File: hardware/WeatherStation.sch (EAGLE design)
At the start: 9 parts, among them X2 XRJK-S-01-6-4-0-9M2

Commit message: fixing schematic v1.1
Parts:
- removed BMP280: (no value), pinhead:PINHD-1X6
- removed EXTERN_PINS: (no value), pinhead:PINHD-1X20
- removed U$1: ESP32DEVKITV1, ESP32-DEVKITV1:ESP32DEVKITV1
- removed X2: XRJK-S-01-6-4-0-9M2, con-xmultiplee:XRJK-S-01-6-4-0-9M2
- removed XB2: XBEE-PRO, maxstream:XBEE-PRO
- added ESP32: ESP32DEVKITV1, ESP32-DEVKITV1:ESP32DEVKITV1
- added J2: RJ11, con-rj_fixed:RJ11
- added JP1: (no value), pinhead:PINHD-1X24
- added ROBOCORE_BEE_V2: XBEE-PRO, maxstream:XBEE-PRO
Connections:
- removed net N$13: U$1.IO16, XB2.DOUT
- removed net N$15: U$1.IO5, XB2.!RESET
- new net N$9: ESP32.IO22, JP1.21
- net N$1: now also ESP32.3V3, ESP32.IO34, J2.3, JP1.1, JP1.11, JP1.17, JP1.5, R3.2, ROBOCORE_BEE_V2.VCC; no longer POWER.1, U$1.VIN
- net N$10: now also ESP32.IO21, JP1.23; no longer BMP280.3, U$1.IO22
- net N$11: now also ESP32.IO17, ROBOCORE_BEE_V2.DIN/!CONFIG; no longer BMP280.4, U$1.IO21
- net N$12: now also J2.2, R2.1; no longer U$1.GND@2, XB2.GND
- net N$14: now also J2.1, R3.1; no longer U$1.IO17, XB2.DIN/!CONFIG
- net N$2: now also ESP32.GND@1, ESP32.IO26, J2.4, JP1.13, JP1.19, JP1.3, JP1.7, R2.2; no longer BMP280.2, EXTERN_PINS.13, EXTERN_PINS.3, EXTERN_PINS.9, R3.2, U$1.GND@1, U$1.IO26, X2.1
- net N$3: now also ESP32.IO35, R1.1; no longer BMP280.1, EXTERN_PINS.1, EXTERN_PINS.11, EXTERN_PINS.15, EXTERN_PINS.5, R2.1, U$1.3V3, X2.2, XB2.VCC
- net N$4: now also ESP32.IO15, JP1.9; no longer R1.1, U$1.IO35
- net N$5: now also ESP32.IO16, ROBOCORE_BEE_V2.DOUT; no longer EXTERN_PINS.7, U$1.IO15
- net N$6: now also ESP32.GND@2, ROBOCORE_BEE_V2.GND; no longer EXTERN_PINS.17, U$1.IO4
- net N$7: now also ESP32.IO4, JP1.15; no longer R2.2, U$1.IO34, X2.4
- net N$8: now also ESP32.VIN, POWER.1; no longer R3.1, X2.3
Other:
- note added: "3V3"
- note added: "3V3/EN"
- note added: "Anemometer + Wind Vane"
- note added: "BMP280 BAROMETER"
- note added: "DATA"
- note added: "DHT11 TEMP/HUM SENSOR"
- note added: "GND"
- note added: "GND/DATA"
- note added: "Lucas José da Cunha"
- note added: "OUT"
- note added: "SCL"
- note added: "SDA"
- note added: "VCC"
- note removed: "DHT11 TEMP/HUM"
- note removed: "LUCAS JOSÉ DA CUNHA"
- moved on the sheet: POWER, R2, R3

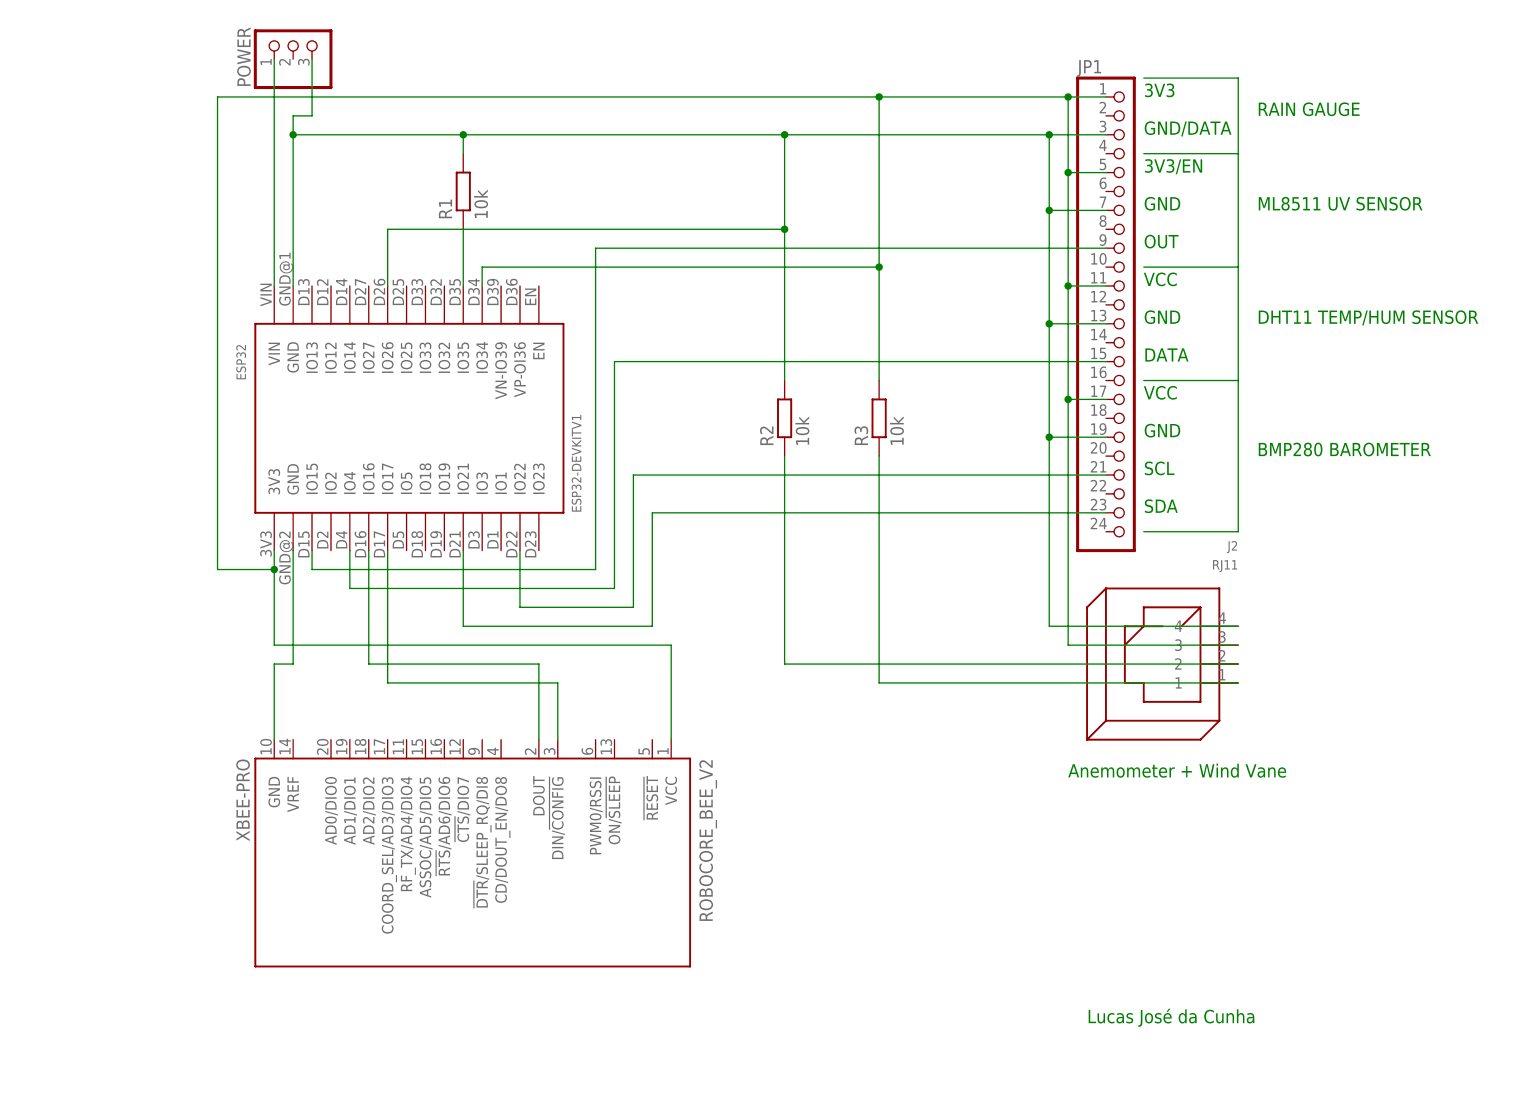
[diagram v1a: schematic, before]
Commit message: changing rain gauge and wind sensor connection
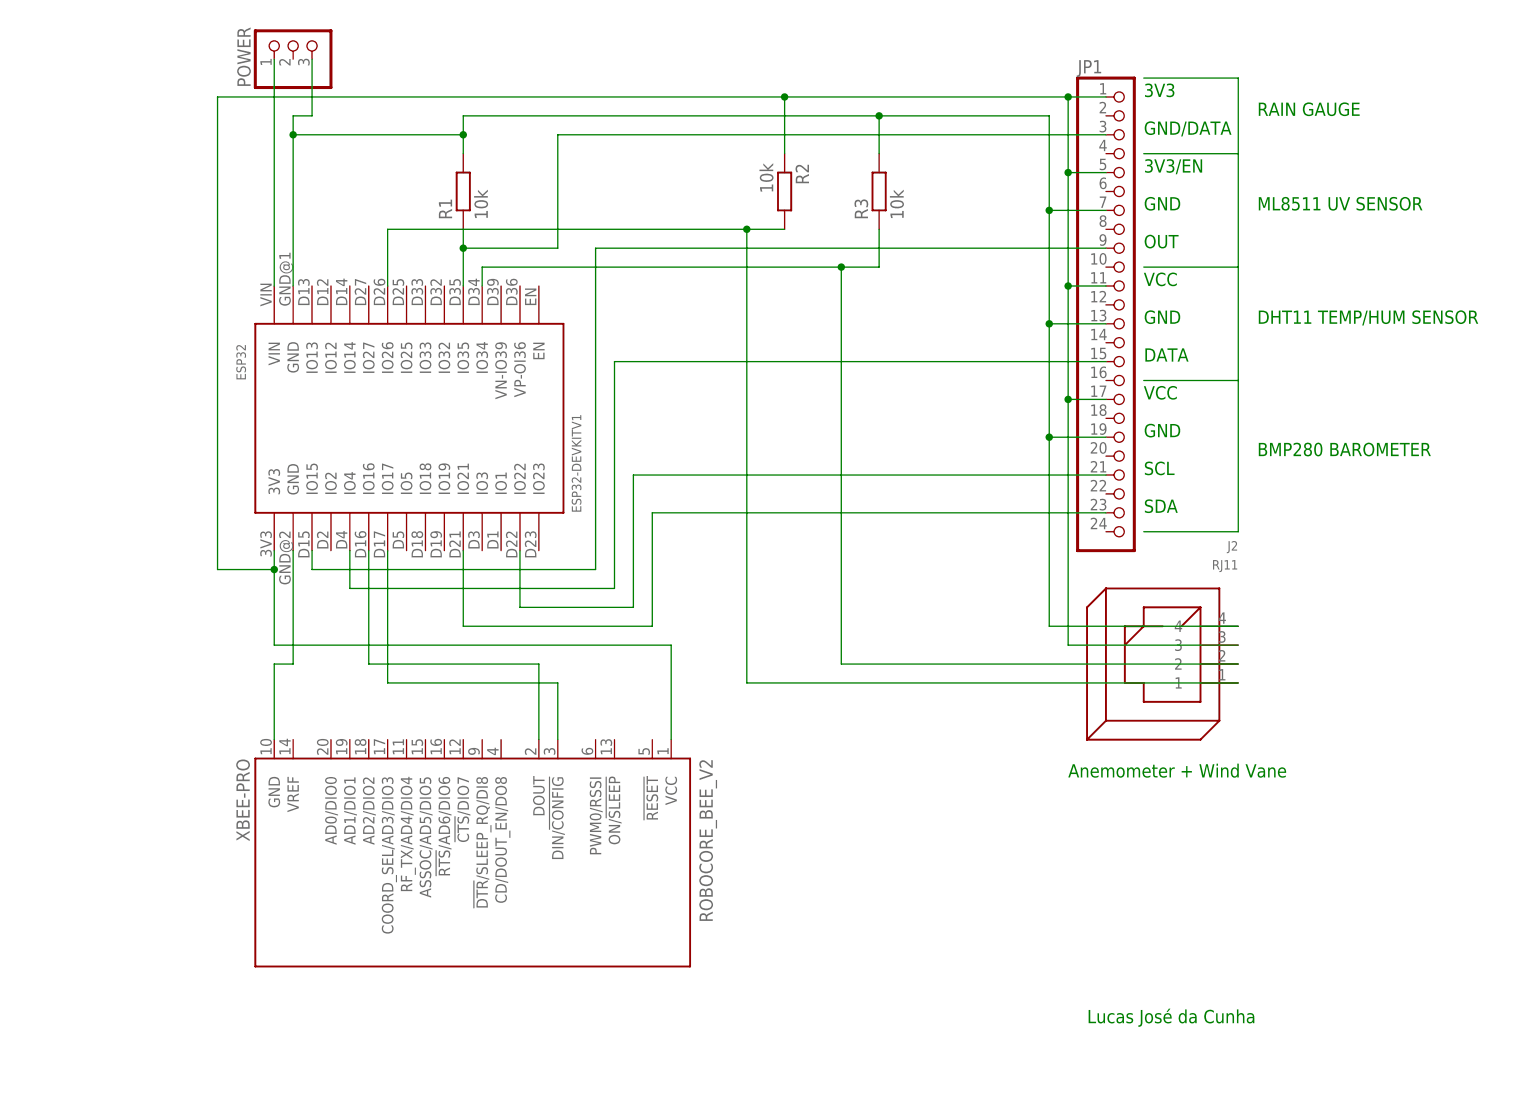
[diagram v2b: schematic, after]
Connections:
- removed net N$14: J2.1, R3.1
- new net N$13: ESP32.GND@1, J2.4, JP1.13, JP1.19, JP1.7, POWER.3, R1.2, R3.2
- net N$1: now also R2.1; no longer ESP32.IO34, R3.2
- net N$12: now also ESP32.IO34, R3.1; no longer R2.1
- net N$2: now also J2.1; no longer ESP32.GND@1, J2.4, JP1.13, JP1.19, JP1.3, JP1.7, POWER.3, R1.2
- net N$3: now also JP1.3
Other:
- moved on the sheet: R2, R3

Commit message: updating schematic, better board, and portuguese fzz
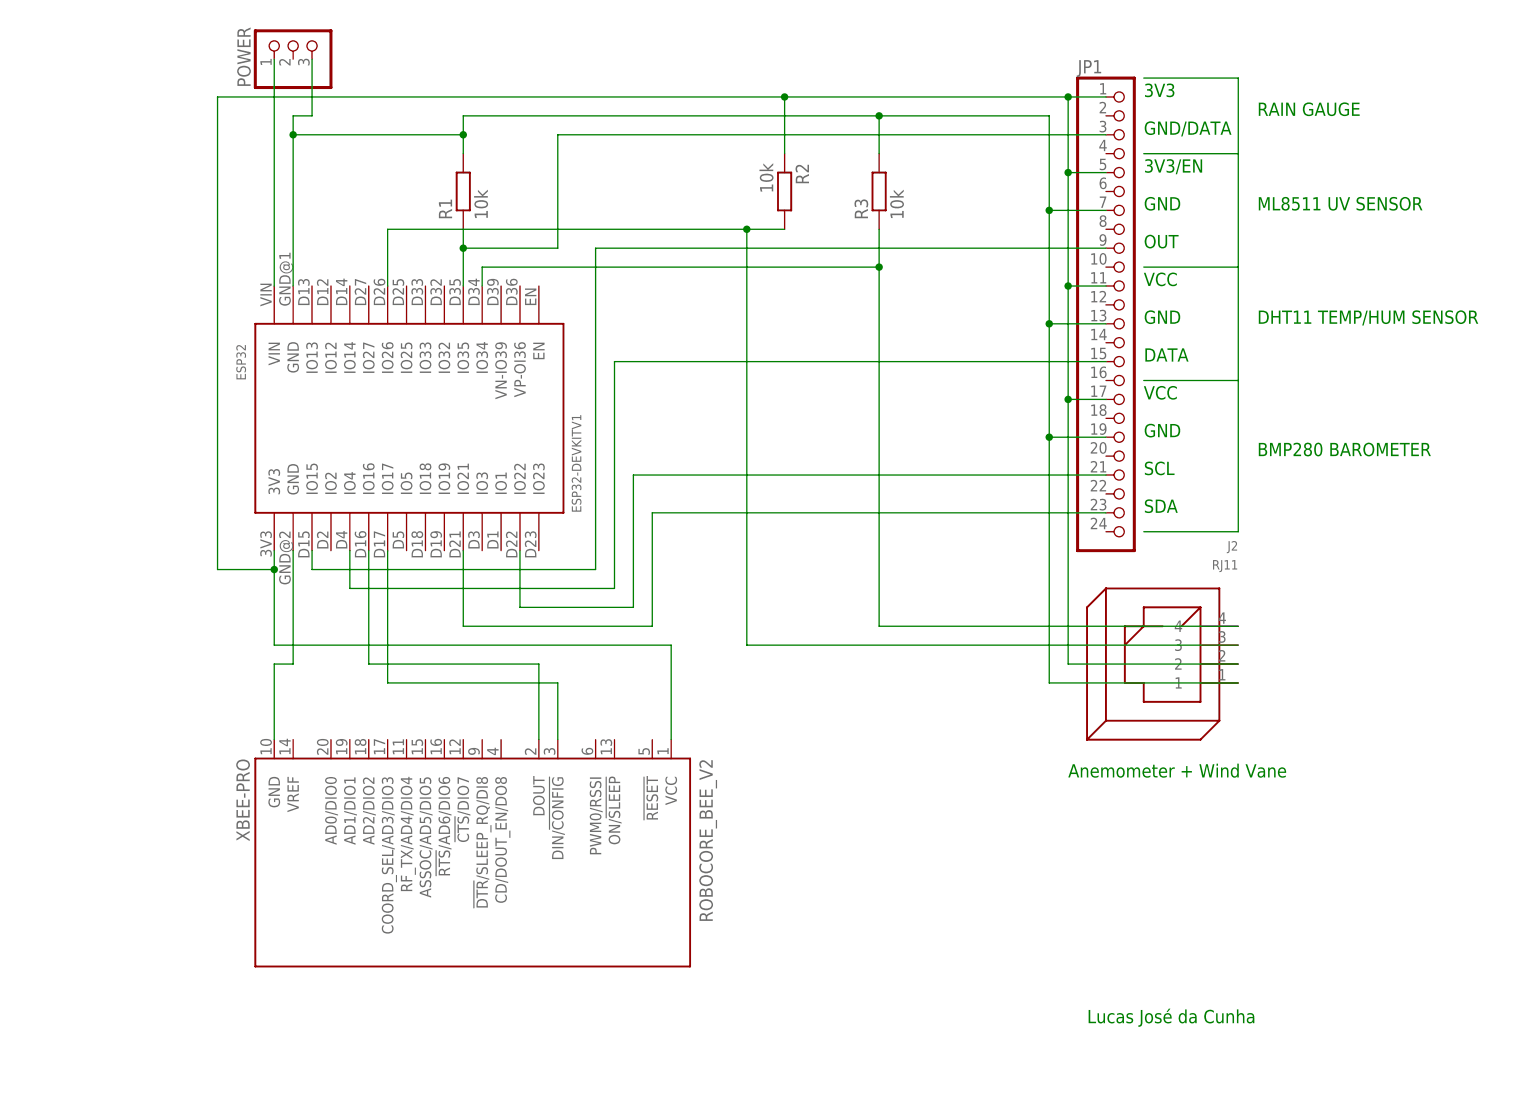
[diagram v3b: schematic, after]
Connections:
- removed net N$12: ESP32.IO34, J2.2, R3.1
- new net N$16: ESP32.IO34, J2.4, R3.1
- net N$1: now also J2.2; no longer J2.3
- net N$13: now also J2.1; no longer J2.4
- net N$2: now also J2.3; no longer J2.1
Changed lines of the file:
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@@
 <wire x1="68.58" y1="66.04" x2="68.58" y2="76.2" width="0.1524" layer="91"/>
 <junction x="68.58" y="76.2"/>
-<wire x1="175.26" y1="66.04" x2="175.26" y2="99.06" width="0.1524" layer="91"/>
-<junction x="175.26" y="99.06"/>
-<pinref part="J2" gate="G$1" pin="3"/>
-<wire x1="175.26" y1="66.04" x2="198.12" y2="66.04" width="0.1524" layer="91"/>
 <pinref part="R2" gate="G$1" pin="1"/>
 <wire x1="137.16" y1="132.08" x2="137.16" y2="139.7" width="0.1524" layer="91"/>
 <junction x="137.16" y="139.7"/>
+<pinref part="J2" gate="G$1" pin="2"/>
+<wire x1="198.12" y1="63.5" x2="175.26" y2="63.5" width="0.1524" layer="91"/>
+<wire x1="175.26" y1="63.5" x2="175.26" y2="99.06" width="0.1524" layer="91"/>
+<junction x="175.26" y="99.06"/>
 </segment>
 </net>
@@
 <wire x1="172.72" y1="93.98" x2="172.72" y2="109.22" width="0.1524" layer="91"/>
 <junction x="172.72" y="109.22"/>
-<wire x1="198.12" y1="68.58" x2="172.72" y2="68.58" width="0.1524" layer="91"/>
-<wire x1="172.72" y1="68.58" x2="172.72" y2="93.98" width="0.1524" layer="91"/>
-<junction x="172.72" y="93.98"/>
-<pinref part="J2" gate="G$1" pin="4"/>
 <wire x1="172.72" y1="137.16" x2="172.72" y2="124.46" width="0.1524" layer="91"/>
 <junction x="172.72" y="124.46"/>
@@
 <wire x1="149.86" y1="132.08" x2="149.86" y2="137.16" width="0.1524" layer="91"/>
 <junction x="149.86" y="137.16"/>
+<pinref part="J2" gate="G$1" pin="1"/>
+<wire x1="198.12" y1="60.96" x2="172.72" y2="60.96" width="0.1524" layer="91"/>
+<wire x1="172.72" y1="60.96" x2="172.72" y2="93.98" width="0.1524" layer="91"/>
+<junction x="172.72" y="93.98"/>
+</segment>
+</net>
+<net name="N$16" class="0">
+<segment>
+<pinref part="ESP32" gate="G$1" pin="IO34"/>
+<wire x1="96.52" y1="114.3" x2="96.52" y2="116.84" width="0.1524" layer="91"/>
+<pinref part="J2" gate="G$1" pin="4"/>
+<wire x1="198.12" y1="68.58" x2="149.86" y2="68.58" width="0.1524" layer="91"/>
+<wire x1="149.86" y1="68.58" x2="149.86" y2="116.84" width="0.1524" layer="91"/>
+<wire x1="149.86" y1="116.84" x2="96.52" y2="116.84" width="0.1524" layer="91"/>
+<pinref part="R3" gate="G$1" pin="1"/>
+<wire x1="149.86" y1="116.84" x2="149.86" y2="121.92" width="0.1524" layer="91"/>
+<junction x="149.86" y="116.84"/>
 </segment>
 </net>
 <net name="N$2" class="0">
 <segment>
+<pinref part="J2" gate="G$1" pin="3"/>
+<wire x1="198.12" y1="66.04" x2="132.08" y2="66.04" width="0.1524" layer="91"/>
+<wire x1="132.08" y1="66.04" x2="132.08" y2="121.92" width="0.1524" layer="91"/>
 <pinref part="ESP32" gate="G$1" pin="IO26"/>
-<wire x1="83.82" y1="114.3" x2="83.82" y2="121.92" width="0.1524" layer="91"/>
-<wire x1="83.82" y1="121.92" x2="132.08" y2="121.92" width="0.1524" layer="91"/>
-<wire x1="132.08" y1="121.92" x2="132.08" y2="60.96" width="0.1524" layer="91"/>
-<pinref part="J2" gate="G$1" pin="1"/>
-<wire x1="132.08" y1="60.96" x2="198.12" y2="60.96" width="0.1524" layer="91"/>
+<wire x1="132.08" y1="121.92" x2="83.82" y2="121.92" width="0.1524" layer="91"/>
+<wire x1="83.82" y1="121.92" x2="83.82" y2="114.3" width="0.1524" layer="91"/>
 <pinref part="R2" gate="G$1" pin="2"/>
-<wire x1="137.16" y1="121.92" x2="132.08" y2="121.92" width="0.1524" layer="91"/>
+<wire x1="132.08" y1="121.92" x2="137.16" y2="121.92" width="0.1524" layer="91"/>
 <junction x="132.08" y="121.92"/>
 </segment>
 </net>
-<net name="N$12" class="0">
-<segment>
-<pinref part="ESP32" gate="G$1" pin="IO34"/>
-<wire x1="96.52" y1="114.3" x2="96.52" y2="116.84" width="0.1524" layer="91"/>
-<wire x1="96.52" y1="116.84" x2="144.78" y2="116.84" width="0.1524" layer="91"/>
-<wire x1="144.78" y1="116.84" x2="144.78" y2="63.5" width="0.1524" layer="91"/>
-<pinref part="J2" gate="G$1" pin="2"/>
-<wire x1="144.78" y1="63.5" x2="198.12" y2="63.5" width="0.1524" layer="91"/>
-<pinref part="R3" gate="G$1" pin="1"/>
-<wire x1="149.86" y1="121.92" x2="149.86" y2="116.84" width="0.1524" layer="91"/>
-<wire x1="149.86" y1="116.84" x2="144.78" y2="116.84" width="0.1524" layer="91"/>
-<junction x="144.78" y="116.84"/>
-</segment>
-</net>
